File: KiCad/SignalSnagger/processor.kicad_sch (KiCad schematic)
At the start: 41 parts, among them J201 Conn_01x02, J202 Conn_01x02, J203 Conn_01x02, J204 Conn_01x02, J205 DB9 Female, P201 ISP/PDI, Q201 BSS84W-7-F, Q202 BSS138W-7-F, SW201 SW_SPST, U201 AVR128DA28, U202 SI5351, X201 SIT1566AC TCO, X202 25 MHz

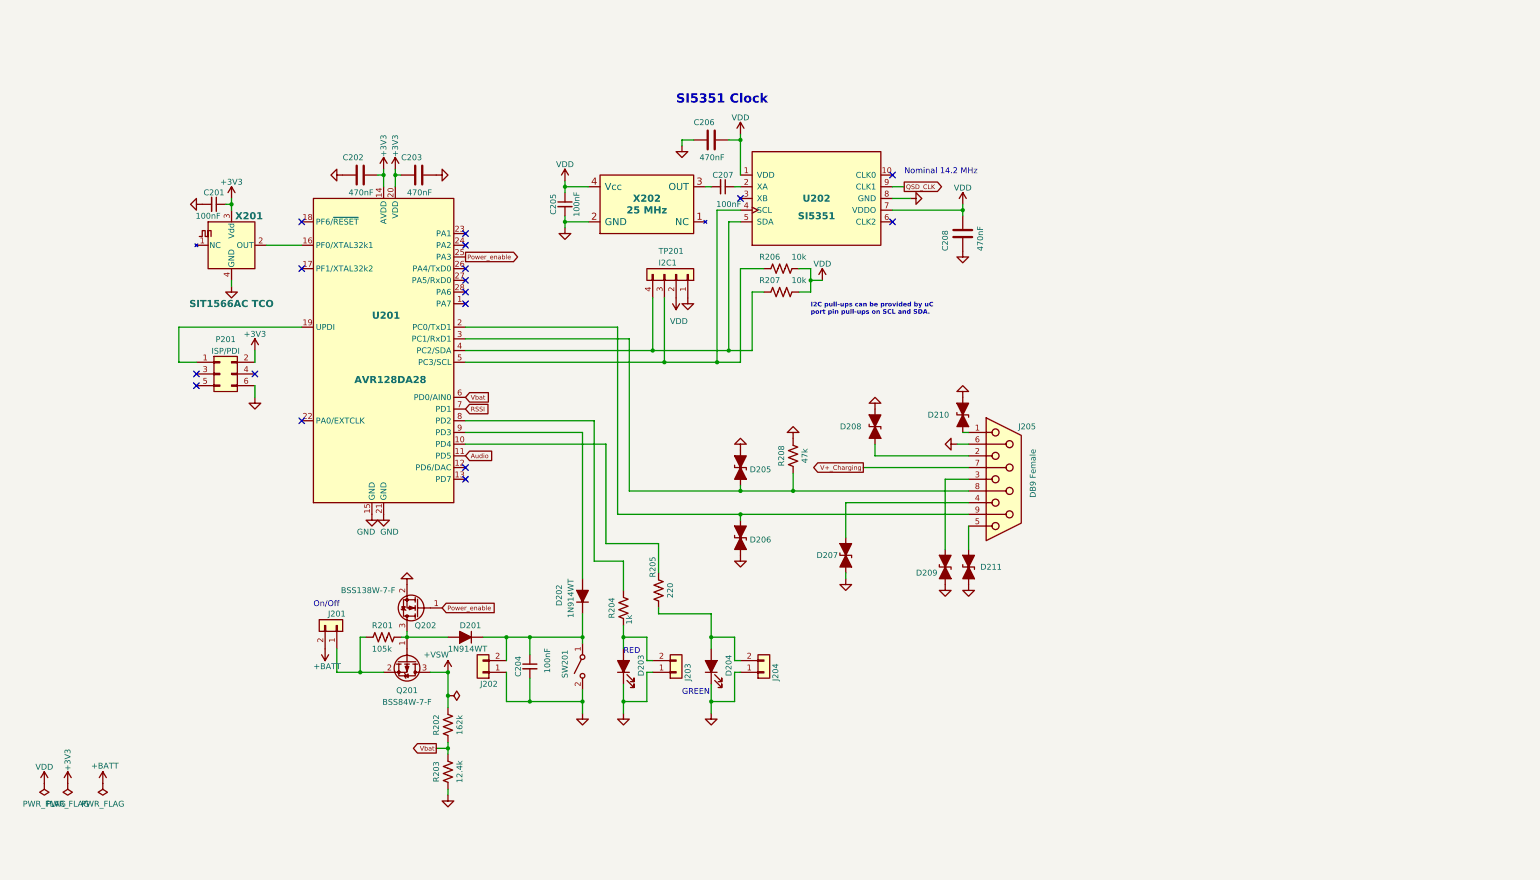
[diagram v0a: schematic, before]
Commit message: Ver 0.15
Schematic changes
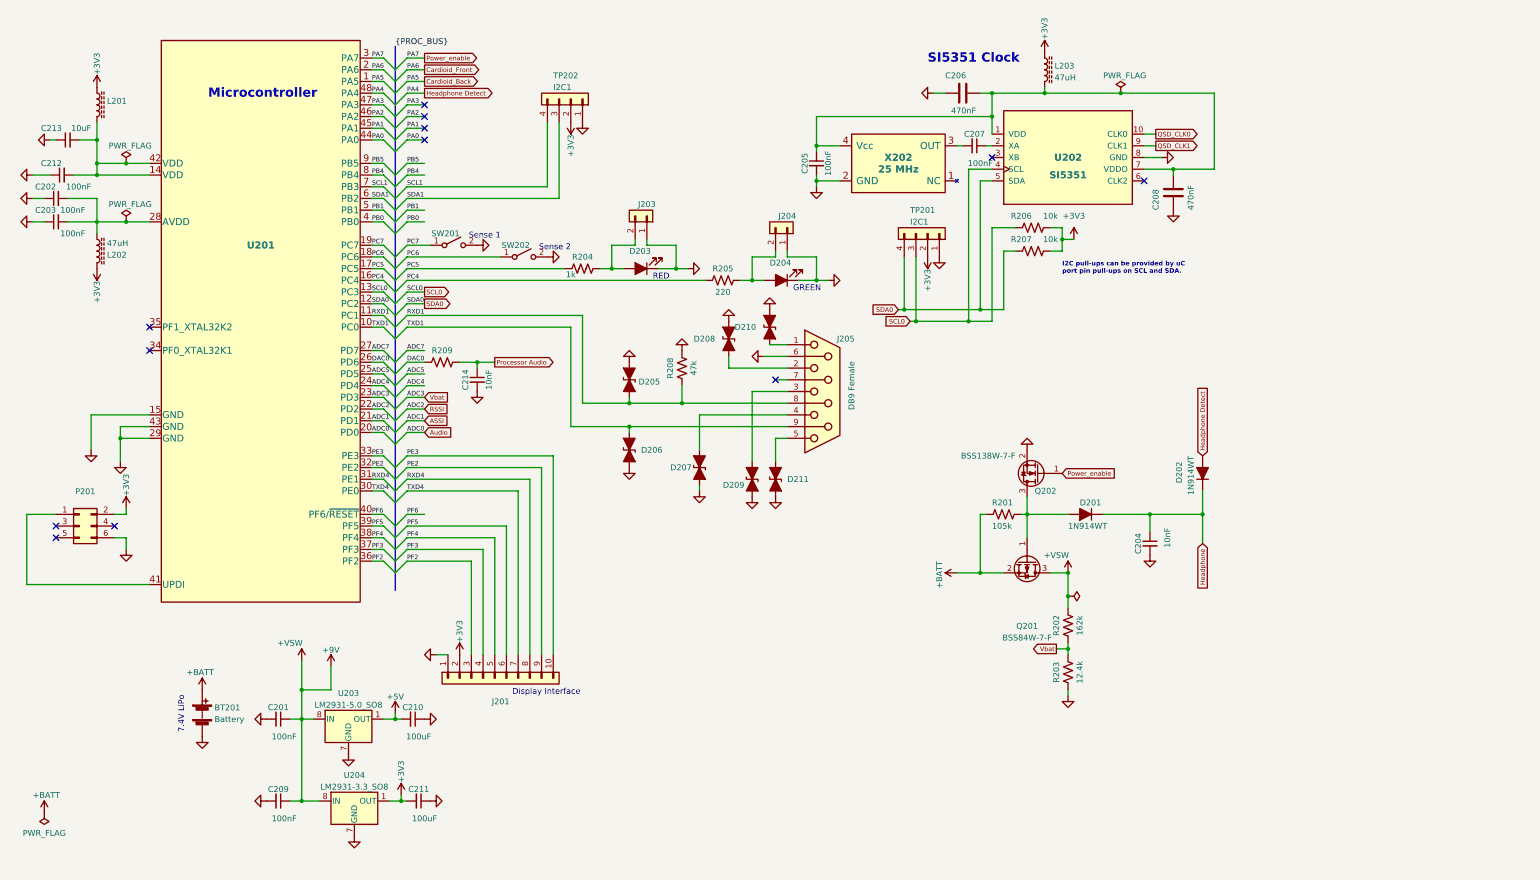
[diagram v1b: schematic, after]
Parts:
- removed C202, C203: 470nF, Capacitor_SMD:C_0805_2012Metric, symbol Device:C
- removed J201, J202: Conn_01x02, Connector_PinSocket_2.54mm:PinSocket_1x02_P2.54mm_Vertical, symbol Connector_Generic:Conn_01x02
- removed U201: AVR128DA28, Package_SO:SOIC-28W_7.5x17.9mm_P1.27mm, symbol MCU_Microchip_AVR:AVR128DA28
- removed X201: SIT1566AC TCO, Oscillator:Oscillator_SMD_SiTime_SIT1566AC-4Pin_BGA, symbol Oscillator:SIT1566AC
- added BT201: Battery, symbol Device:Battery
- added C202, C203, C212: 100nF, Capacitors_SMD:C_0805, symbol Device:C_Small
- added C209: 100nF, Capacitor_SMD:C_0805_2012Metric, symbol Device:C_Small
- added C210, C211: 100uF, Capacitor_SMD:C_0805_2012Metric, symbol Device:C_Small
- added C213: 10uF, Capacitors_SMD:C_0805, symbol Device:C_Small
- added C214: 10nF, Capacitor_SMD:C_0805_2012Metric, symbol Device:C_Small
- added J201: Conn_01x10, Connector_PinHeader_2.54mm:PinHeader_1x10_P2.54mm_Vertical, symbol Connector_Generic:Conn_01x10
- added L201: (no value), symbol Device:L_Ferrite
- added L202, L203: 47uH, symbol Device:L_Ferrite
- added R209: (no value), Resistor_SMD:R_0805_2012Metric, symbol Device:R_Small_US
- added SW202: SW_SPST, Button_Switch_SMD:SW_SPST_TL3305A, symbol Switch:SW_SPST
- added TP202: I2C1, Connector_PinHeader_2.54mm:PinHeader_1x04_P2.54mm_Vertical, symbol Connector_Generic:Conn_01x04
- added U201: (no value), symbol MCU_Microchip_AVR:AVR128DA48-I_PT-MCU_Microchip_AVR
- added U203: LM2931-5.0_SO8, Package_SO:SOIC-8_3.9x4.9mm_P1.27mm, symbol Regulator_Linear:LM2931-5.0_SO8
- added U204: LM2931-3.3_SO8, Package_SO:SOIC-8_3.9x4.9mm_P1.27mm, symbol Regulator_Linear:LM2931-5.0_SO8
- C204: value 100nF -> 10nF
- P201: value ISP/PDI -> (none); footprint Connector_PinHeader_2.54mm:PinHeader_2x03_P2.54mm_Vertical_SMD -> (none); Digi-Key Part No. 609-3487-1-ND -> (none); LCSC Part Number C178294 -> (none); Link https://www.digikey.com/products/en?keywords=609-3487-1-ND -> (none); Manufacturer Amphenol ICC (FCI) -> (none); Manufacturer PN 95278-101A06LF -> (none)
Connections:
- net +3V3: now also R206.2, R207.2, TP201.2 (Pin_2), C211.2, J201.2 (Pin_2), L201.1, L202.1, L203.1, TP202.2 (Pin_2), U204.1 (OUT); no longer C201.1
- net +BATT: now also Q201.2 (S), R201.2, BT201.2 (+)
- net Audio: now also U201.20 (PD0)
- net GND: now also BT201.1 (-), C202.1, C203.1, C209.2, C210.1, C211.1, C212.1, C213.1, C214.2, J201.1 (Pin_1), SW202.2 (B), TP202.1 (Pin_1), U201.15 (GND), U201.29 (GND), U201.43 (GND), U203.2 (GND), U203.3 (GND), U203.6 (GND), U203.7 (GND), U204.2 (GND), U204.3 (GND), U204.6 (GND), U204.7 (GND)
- net Power_enable: now also U201.3 (PA7)
- net RSSI: now also U201.22 (PD2)
- net Vbat: now also U201.23 (PD3)
- net at D203.2 (A), J203.2 (Pin_2): now also R204.2; no longer R204.1
- net at D204.2 (A), J204.2 (Pin_2): now also R205.2; no longer R205.1
- net RXD1: now reaches D205.2 (A2), J205.8, R208.1
- net RXD1: now also U201.11 (PC1)
- net Headphone: now reaches C204.1, D201.1 (K), D202.1 (K)
- net Headphone: no longer SW201.1 (A)
- net at P201.1 (Pin_1): now also U201.41 (UPDI)
- net SDA0: now reaches R207.1, TP201.4 (Pin_4), U202.5 (SDA)
- net SDA0: now also U201.12 (PC2)
- net TXD1: now reaches D206.1 (A1), J205.9
- net TXD1: now also U201.10 (PC0)
- net SCL0: now reaches R206.1, TP201.3 (Pin_3), U202.4 (SCL)
- net SCL0: now also U201.13 (PC3)
- net Headphone Detect: now reaches D202.2 (A)
- net Headphone Detect: now also U201.48 (PA4)
- net QSD_CLK0: now reaches U202.10 (CLK0)
- net +VSW renamed +9V
- net +9V: now also C201.1, C209.1, U203.8 (IN), U204.8 (IN)
- net QSD_CLK renamed QSD_CLK1
- net V+_Charging: no longer names the net of J205.7
- net VDD: no longer names the net of C205.1, C206.1, C208.1, U202.1 (VDD), U202.7 (VDDO), X202.4 (Vcc)
- net VDD: now also L203.2; no longer R206.2, R207.2, TP201.2 (Pin_2)
- new net: C212.2, C213.2, L201.2, U201.14 (VDD), U201.42 (VDD)
- new net: C202.2, C203.2, L202.2, U201.28 (AVDD)
- new net +5V: C210.2, U203.1 (OUT)
- new net ADC4: U201.24 (PD4)
- new net ADC5: U201.25 (PD5)
- new net ADC7: U201.27 (PD7)
- new net ASSI: U201.21 (PD1)
- new net Cardioid_Back: U201.1 (PA5)
- new net Cardioid_Front: U201.2 (PA6)
- new net DAC0: R209.1, U201.26 (PD6)
- new net PA0: U201.44 (PA0)
- new net PA1: U201.45 (PA1)
- new net PA2: U201.46 (PA2)
- new net PA3: U201.47 (PA3)
- new net PB0: U201.4 (PB0)
- new net PB1: U201.5 (PB1)
- new net PB4: U201.8 (PB4)
- new net PB5: U201.9 (PB5)
- new net PC4: R205.1, U201.16 (PC4)
- new net PC5: R204.1, U201.17 (PC5)
- new net PC6: SW202.1 (A), U201.18 (PC6)
- new net PC7: SW201.1 (A), U201.19 (PC7)
- new net PE2: J201.9 (Pin_9), U201.32 (PE2)
- new net PE3: J201.10 (Pin_10), U201.33 (PE3)
- new net PF2: J201.3 (Pin_3), U201.36 (PF2)
- new net PF3: J201.4 (Pin_4), U201.37 (PF3)
- new net PF4: J201.5 (Pin_5), U201.38 (PF4)
- new net PF5: J201.6 (Pin_6), U201.39 (PF5)
- new net PF6: U201.40 (PF6/~{RESET})
- new net Processor Audio: C214.1, R209.2
- new net RXD4: J201.8 (Pin_8), U201.31 (PE1)
- new net SCL1: TP202.4 (Pin_4), U201.7 (PB3)
- new net SDA1: TP202.3 (Pin_3), U201.6 (PB2)
- new net TXD4: J201.7 (Pin_7), U201.30 (PE0)
- no-connect marks 17 -> 12
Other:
- note added: "7.4V LiPo"
- note added: "Display Interface"
- note added: "Microcontroller"
- note added: "Sense 1"
- note added: "Sense 2"
- note removed: "Nominal 14.2 MHz"
- note removed: "On/Off"
- moved on the sheet: C204, C205, C206, C207, C208, D201, D202, D203, D204, D205, D206, D207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

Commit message: Schematic Updates
Added display and rotary encoder
Added Jerry's changes based on testing
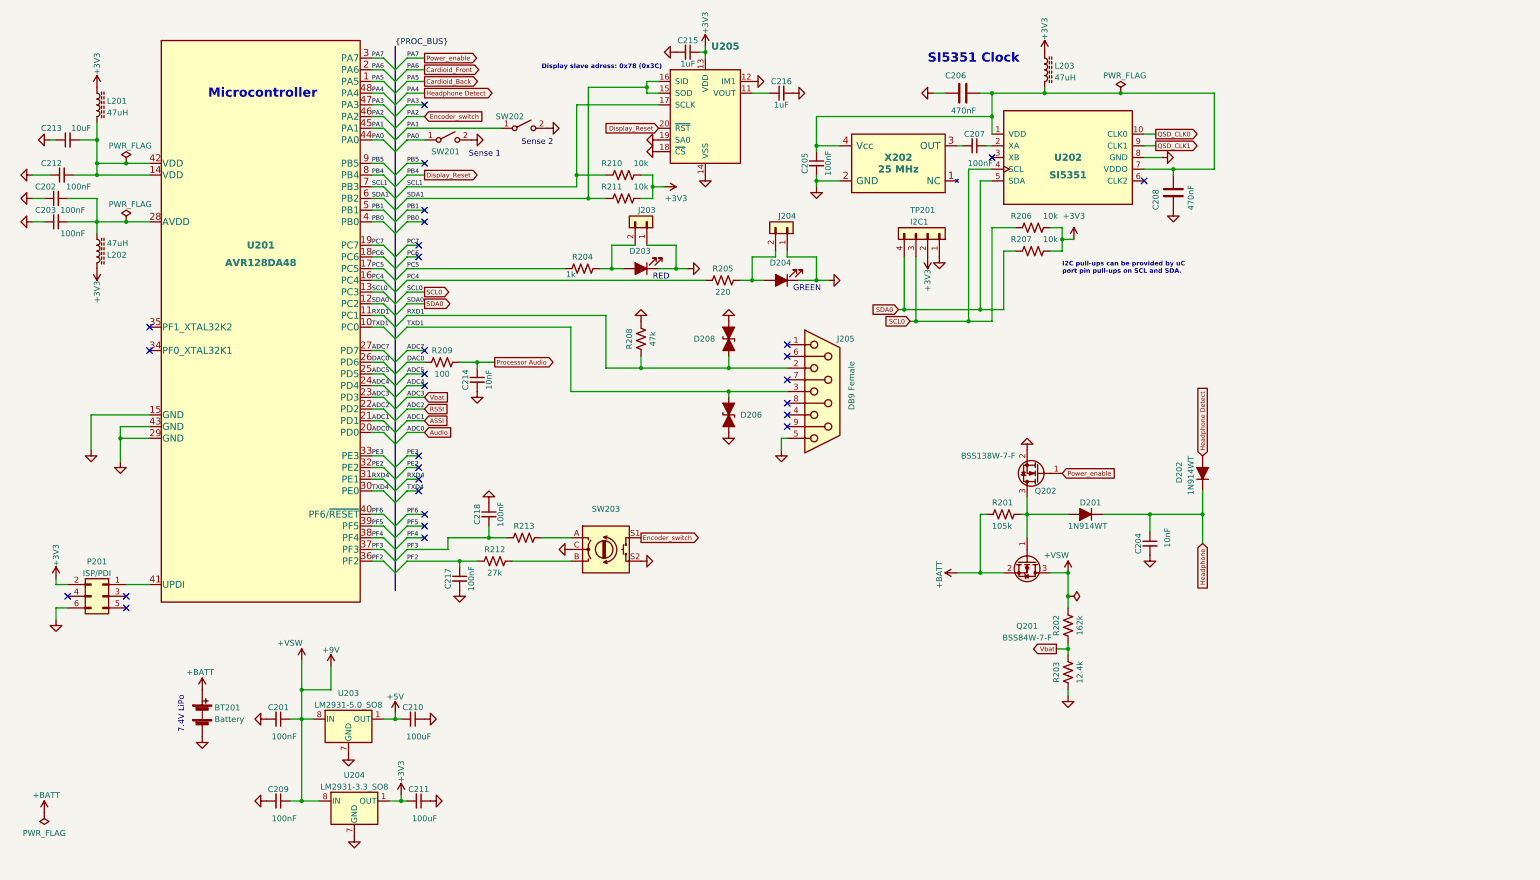
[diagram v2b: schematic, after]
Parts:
- removed D205, D207, D209, D210, D211: ESD9B5.0ST5G_1, Diode_SMD:D_0603_1608Metric, symbol Diode:ESD9B5.0ST5G_1
- removed J201: Conn_01x10, Connector_PinHeader_2.54mm:PinHeader_1x10_P2.54mm_Vertical, symbol Connector_Generic:Conn_01x10
- removed TP202: I2C1, Connector_PinHeader_2.54mm:PinHeader_1x04_P2.54mm_Vertical, symbol Connector_Generic:Conn_01x04
- added C215, C216: 1uF, Capacitor_SMD:C_0805_2012Metric, symbol Device:C_Small
- added C217, C218: 100nF, Capacitor_SMD:C_0805_2012Metric, symbol Device:C_Small
- added R210, R211: 10k, Capacitor_SMD:C_0805_2012Metric, symbol Device:R_Small_US
- added R212: 27k, Resistor_SMD:R_0805_2012Metric, symbol Device:R_Small_US
- added R213: (no value), Resistor_SMD:R_0805_2012Metric, symbol Device:R_Small_US
- added SW203: (no value), symbol Device:RotaryEncoder_Switch
- added U205: (no value), Display:EA_DOGS104X-A, symbol Display_Graphic:EA_DOGS104B-A
- L201: value (none) -> 47uH
- P201: value (none) -> ISP/PDI
- R209: value (none) -> 100
- U201: value (none) -> AVR128DA48; footprint (none) -> Housings_QFP:TQFP-48_7x7mm_Pitch0.5mm_AVR128DA48
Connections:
- net +3V3: now also C215.1, R210.2, R211.2, U205.13 (VDD)
- net GND: now also J205.5, C215.2, C216.2, C217.2, C218.1, SW203.C, SW203.S2, U205.12 (IM1), U205.14 (VSS), U205.18 (~{CS}), U205.19 (SA0); no longer J205.6
- net PA0: now also SW201.1 (A)
- net PA1: now also SW202.1 (A)
- net PC6: no longer SW202.1 (A)
- net PC7: no longer SW201.1 (A)
- net PF2: now also C217.1, R212.1
- net PF3: now also C218.2, R213.1
- net RXD1: now also D208.2 (A2), J205.2; no longer J205.8
- net SCL1: now also R210.1, U205.17 (SCLK)
- net SDA1: now also R211.1, U205.15 (SOD), U205.16 (SID)
- net TXD1: now also J205.3; no longer J205.9
- net PA2 renamed Encoder_switch
- net Encoder_switch: now also SW203.S1
- net PB4 renamed Display_Reset
- net Display_Reset: now also U205.20 (~{RST})
- new net: C216.1, U205.11 (VOUT)
- new net: R213.2, SW203.A
- new net: R212.2, SW203.B
- no-connect marks 12 -> 29
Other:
- note added: "Display slave adress: 0x78 (0x3C)"
- note removed: "Display Interface"
- moved on the sheet: D206, J203, P201, R208, SW201, SW202

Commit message: Schematic Updates
Rev 0.18
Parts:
- added L204: 47uH, symbol Device:L_Ferrite
- R210, R211: value 10k -> NP
- R213: value (none) -> 27k
- SW203: value (none) -> PEC12R-4225F-S0024
- U205: value (none) -> EA_DOGS104W-A
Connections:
- net ADC4 is gone; now on net Vbat: U201.24 (PD4)
- net +3V3: now also L204.1; no longer C215.1, U205.13 (VDD)
- net +9V: no longer Q201.3 (D), R202.2
- net ASSI: now also U201.22 (PD2); no longer U201.21 (PD1)
- net RSSI: now also U201.23 (PD3); no longer U201.22 (PD2)
- net SCL0: now also U205.17 (SCLK)
- net SCL1: no longer U205.17 (SCLK)
- net SDA0: now also U205.15 (SOD), U205.16 (SID)
- net SDA1: no longer U205.15 (SOD), U205.16 (SID)
- net Vbat: no longer U201.23 (PD3)
- net at C212.2, L201.2, U201.14 (VDD)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: now also C202.2; no longer C213.2
- net at C203.2, L202.2, U201.28 (AVDD): now also C213.2; no longer C202.2
- net Audio renamed Audio I
- new net: C215.1, L204.2, U205.13 (VDD)
- new net +VSW: Q201.3 (D), R202.2
- new net Audio Q: U201.21 (PD1)
- no-connect marks 29 -> 28
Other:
- moved on the sheet: BT201, C201, C202, C203, C204, C205, C206, C207, C208, C209, C210, C211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

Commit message: Schematic Tweaks
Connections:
- net +9V is gone; now on net +VSW: C201.1, C209.1, U203.8 (IN), U204.8 (IN)
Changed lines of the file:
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@@
+    (pin "1")
+  )
+  (symbol (lib_id "power:+VSW") (at 132.08 167.64 0) (unit 1)
+    (in_bom yes) (on_board yes)
+    (property "Reference" "#PWR0145" (id 0) (at 132.08 171.45 0)
+      (effects (font (size 1.27 1.27)) hide)
+    )
+    (property "Value" "+VSW" (id 1) (at 129.54 163.83 0))
+    (property "Footprint" "" (id 2) (at 132.08 167.64 0)
+      (effects (font (size 1.27 1.27)) hide)
+    )
+    (property "Datasheet" "" (id 3) (at 132.08 167.64 0)
+      (effects (font (size 1.27 1.27)) hide)
+    )
     (pin "1")
   )
@@
     (pin "1")
     (pin "2")
-  )
-  (symbol (lib_id "power:PWR_FLAG") (at 26.67 190.5 0) (mirror x) (unit 1)
-    (in_bom yes) (on_board yes) (fields_autoplaced)
-    (property "Reference" "#FLG0104" (id 0) (at 26.67 192.405 0)
-      (effects (font (size 1.27 1.27)) hide)
-    )
-    (property "Value" "PWR_FLAG" (id 1) (at 26.67 194.9434 0))
-    (property "Footprint" "" (id 2) (at 26.67 190.5 0)
-      (effects (font (size 1.27 1.27)) hide)
-    )
-    (property "Datasheet" "~" (id 3) (at 26.67 190.5 0)
-      (effects (font (size 1.27 1.27)) hide)
-    )
-    (pin "1")
   )
   (symbol (lib_id "power:GND") (at 109.22 185.42 0) (unit 1)
@@
     (pin "1")
   )
-  (symbol (lib_id "power:+9V") (at 26.67 190.5 0) (unit 1)
-    (in_bom yes) (on_board yes) (fields_autoplaced)
-    (property "Reference" "#PWR0143" (id 0) (at 26.67 194.31 0)
-      (effects (font (size 1.27 1.27)) hide)
-    )
-    (property "Value" "+9V" (id 1) (at 26.67 186.9242 0))
-    (property "Footprint" "" (id 2) (at 26.67 190.5 0)
-      (effects (font (size 1.27 1.27)) hide)
-    )
-    (property "Datasheet" "" (id 3) (at 26.67 190.5 0)
-      (effects (font (size 1.27 1.27)) hide)
-    )
-    (pin "1")
-  )
   (symbol (lib_id "power:GND") (at 17.78 66.04 270) (unit 1)
     (in_bom yes) (on_board yes) (fields_autoplaced)
@@
     (pin "2")
   )
-  (symbol (lib_id "power:+9V") (at 132.08 167.64 0) (unit 1)
-    (in_bom yes) (on_board yes) (fields_autoplaced)
-    (property "Reference" "#PWR0245" (id 0) (at 132.08 171.45 0)
-      (effects (font (size 1.27 1.27)) hide)
-    )
-    (property "Value" "+9V" (id 1) (at 132.08 164.0642 0))
-    (property "Footprint" "" (id 2) (at 132.08 167.64 0)
-      (effects (font (size 1.27 1.27)) hide)
-    )
-    (property "Datasheet" "" (id 3) (at 132.08 167.64 0)
-      (effects (font (size 1.27 1.27)) hide)
-    )
-    (pin "1")
-  )
   (symbol (lib_id "power:GND") (at 134.62 147.32 270) (mirror x) (unit 1)

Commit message: Schematic Updates
First cut at prototype design
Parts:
- removed L201, L203, L204: 47uH, symbol Device:L_Ferrite
- removed U203: LM2931-5.0_SO8, Package_SO:SOIC-8_3.9x4.9mm_P1.27mm, symbol Regulator_Linear:LM2931-5.0_SO8
- removed U204: LM2931-3.3_SO8, Package_SO:SOIC-8_3.9x4.9mm_P1.27mm, symbol Regulator_Linear:LM2931-5.0_SO8
- added C219: 10nF, Capacitor_SMD:C_0805_2012Metric, symbol Device:C_Small
- added C220: (no value), Capacitor_SMD:C_0805_2012Metric, symbol Device:C_Small
- added U203: (no value), symbol Regulator_Linear:LP2985-3.3
- added U204: (no value), Package_TO_SOT_SMD:SOT-23-5, symbol Regulator_Linear:LP2985-3.3
- C211: value 100uF -> (none)
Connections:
- net +3V3: now also C202.2, C205.1, C206.1, C208.1, C212.2, C215.1, U201.14 (VDD), U201.42 (VDD), U202.1 (VDD), U202.7 (VDDO), U205.13 (VDD), X202.4 (Vcc), U204.5 (VOUT)
- net +5V: now also U203.5 (VOUT)
- net +VSW: now also U203.1 (VIN), U204.1 (VIN), U204.3 (ON/~{OFF})
- net GND: now also C219.2, C220.2, U203.2 (GND); no longer C202.1, C203.1, C205.2, C206.2, C208.2, C209.2, C211.1, C212.1, C213.1, C214.2, C215.2, C216.2, C217.2, C218.1, D203.1 (K), D204.1 (K), D206.2 (A2), D208.1 (A1), J203.1 (Pin_1), J204.1 (Pin_1), J205.5, P201.6 (Pin_6), R208.2, SW201.2 (B), SW202.2 (B), SW203.C, SW203.S2, TP201.1 (Pin_1), U201.15 (GND), U201.29 (GND), U201.43 (GND), U202.8 (GND), U205.12 (IM1), U205.14 (VSS), U205.18 (~{CS}), U205.19 (SA0), X202.2 (GND)
- new net: C219.1, U204.4 (BP)
- new net: C220.1, U203.4 (BP)
- new net GNDD: C202.1, C203.1, C205.2, C206.2, C208.2, C209.2, C211.1, C212.1, C213.1, C214.2, C215.2, C216.2, C217.2, C218.1, D203.1 (K), D204.1 (K), D206.2 (A2), D208.1 (A1), J203.1 (Pin_1), J204.1 (Pin_1), J205.5, P201.6 (Pin_6), R208.2, SW201.2 (B), SW202.2 (B), SW203.C, SW203.S2, TP201.1 (Pin_1), U201.15 (GND), U201.29 (GND), U201.43 (GND), U202.8 (GND), U204.2 (GND), U205.12 (IM1), U205.14 (VSS), U205.18 (~{CS}), U205.19 (SA0), X202.2 (GND)
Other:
- moved on the sheet: BT201, C201, C209, C210, C211
